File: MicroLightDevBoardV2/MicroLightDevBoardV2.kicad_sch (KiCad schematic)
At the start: 65 parts, among them J1 Conn_01x05_Socket, J10 Conn_01x01_Socket, J11 Conn_01x05_Socket, J12 Conn_01x02_Socket, J13 Conn_01x04_Socket, J14 Conn_01x04_Socket, J15 Conn_01x05_Socket, J16 Conn_01x01_Socket, J17 Conn_01x04_Socket, J18 Conn_01x04_Socket, J19 Conn_01x04_Socket, J2 Conn_01x05_Socket, J20 Conn_01x04_Socket, J21 Conn_01x04_Socket, J22 Conn_01x04_Socket, J23 Conn_01x03_Socket, J24 Conn_01x03_Socket, J25 Conn_01x04_Socket, J26 Conn_01x04_Socket, J27 Conn_01x02_Socket, J28 Conn_01x02_Socket, J29 Conn_01x02_Socket, J3 Conn_01x05_Socket, J30 Conn_01x02_Socket, J31 Conn_01x01_Socket, J32 Conn_01x06_Socket, J33 Conn_01x04_Socket, J4 Conn_01x05_Socket, J5 Conn_01x02_Socket, J6 Conn_01x02_Socket, J7 TYPE-C-31-M-12, J8 Conn_01x02_Socket, J9 Conn_01x02_Socket, U1 BQ25628RYKR, U2 ATtiny3226-M, U3 S-85S1AB33-I6T1U, U4 USBLC6-2P6, U5 MC3479

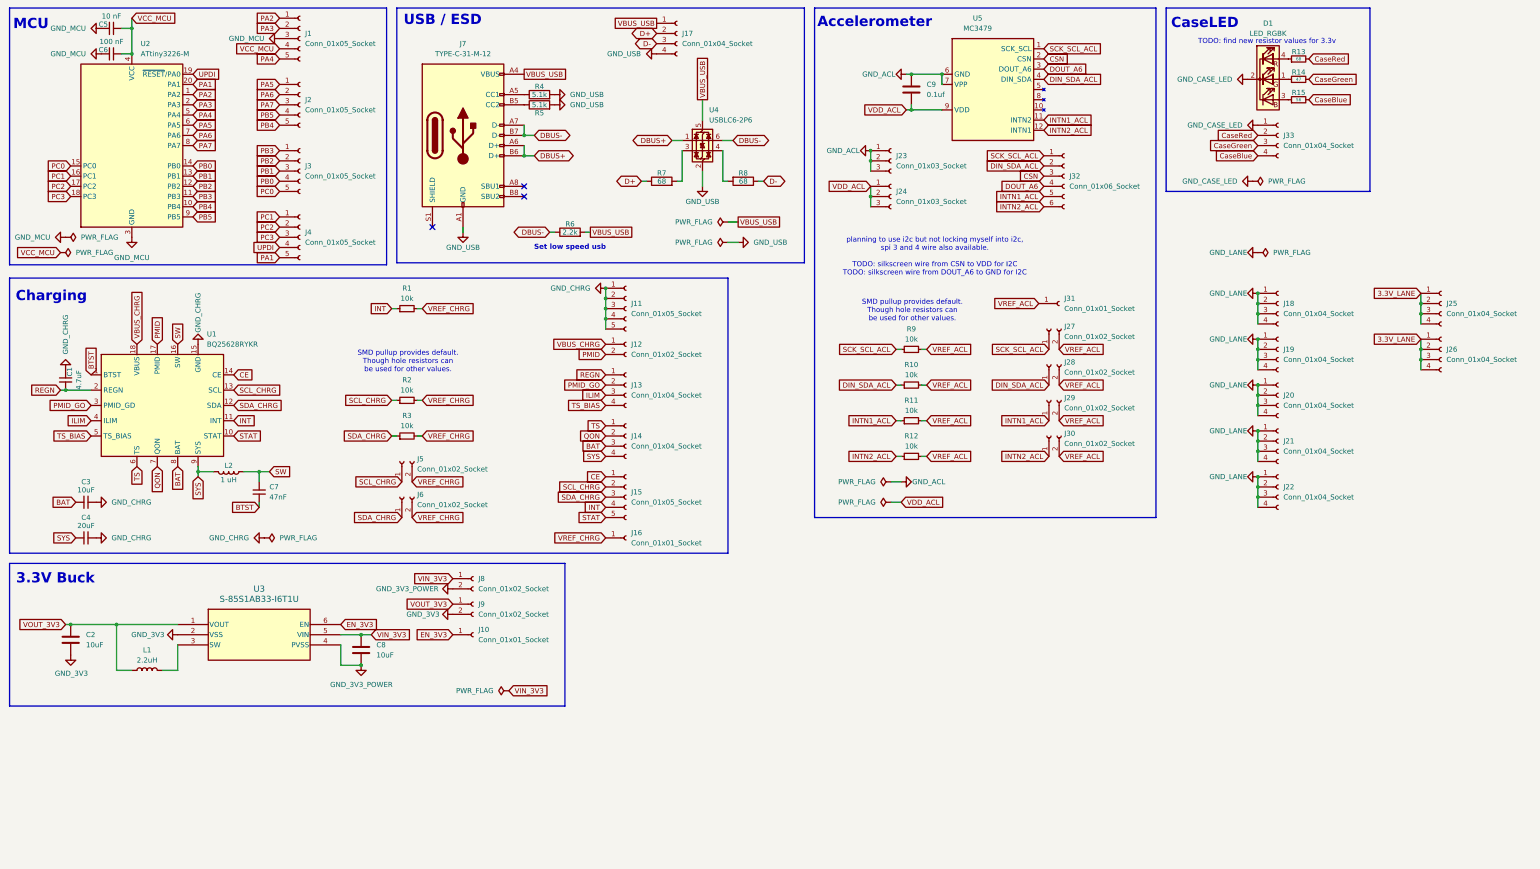
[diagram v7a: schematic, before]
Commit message: add buttons to pcb, add breadboard like expansion sockets
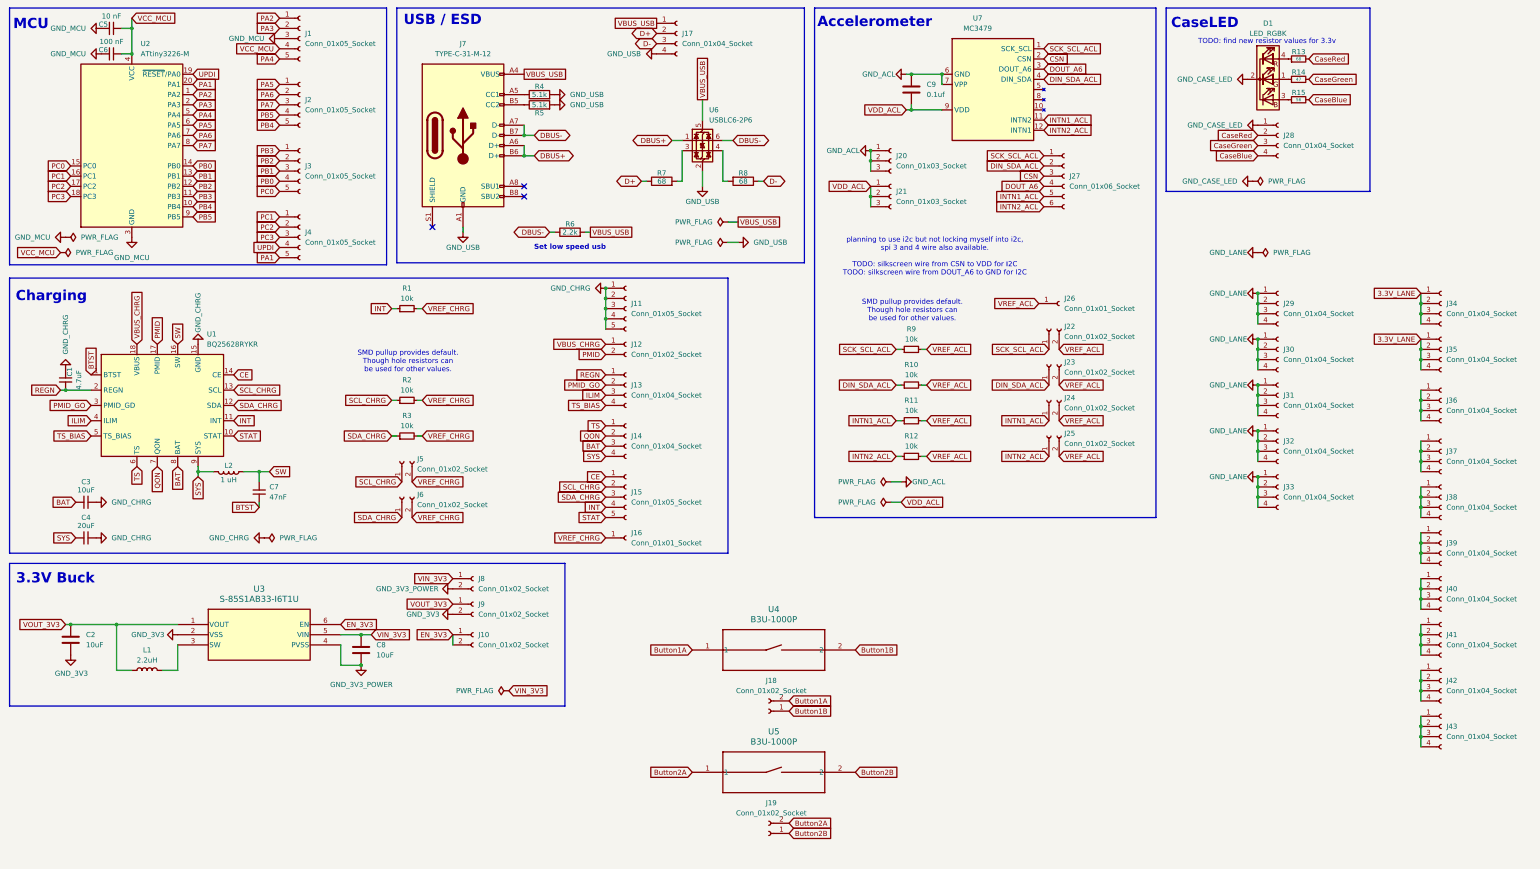
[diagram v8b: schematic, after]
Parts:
- removed J10: Conn_01x01_Socket, Connector_PinSocket_2.54mm:PinSocket_1x01_P2.54mm_Vertical, symbol Connector:Conn_01x01_Socket
- added J10, J18, J19: Conn_01x02_Socket, Connector_PinSocket_2.54mm:PinSocket_1x02_P2.54mm_Vertical, symbol Connector:Conn_01x02_Socket
- added J36, J37, J38, J39, J40, J41, J42, J43: Conn_01x04_Socket, Connector_PinSocket_2.54mm:PinSocket_1x04_P2.54mm_Vertical, symbol Connector:Conn_01x04_Socket
- added U4, U5: B3U-1000P, B3U-1000P, symbol MicroLightDevBoard:B3U-1000P
- renumbered J23 to J20, J24 to J21, J27 to J22, J28 to J23, J29 to J24, J30 to J25, J31 to J26, J32 to J27, J33 to J28, J18 to J29, J19 to J30, J20 to J31, J21 to J32, J22 to J33, J25 to J34, J26 to J35, U4 to U6, U5 to U7
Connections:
- net EN_3V3: now also J10.1 (Pin_1), J10.2 (Pin_2)
- new net: J41.1 (Pin_1), J41.2 (Pin_2), J41.3 (Pin_3), J41.4 (Pin_4)
- new net: J39.1 (Pin_1), J39.2 (Pin_2), J39.3 (Pin_3), J39.4 (Pin_4)
- new net: J38.1 (Pin_1), J38.2 (Pin_2), J38.3 (Pin_3), J38.4 (Pin_4)
- new net: J40.1 (Pin_1), J40.2 (Pin_2), J40.3 (Pin_3), J40.4 (Pin_4)
- new net: J36.1 (Pin_1), J36.2 (Pin_2), J36.3 (Pin_3), J36.4 (Pin_4)
- new net: J42.1 (Pin_1), J42.2 (Pin_2), J42.3 (Pin_3), J42.4 (Pin_4)
- new net: J37.1 (Pin_1), J37.2 (Pin_2), J37.3 (Pin_3), J37.4 (Pin_4)
- new net: J43.1 (Pin_1), J43.2 (Pin_2), J43.3 (Pin_3), J43.4 (Pin_4)
- new net Button1A: J18.2 (Pin_2), U4.1
- new net Button1B: J18.1 (Pin_1), U4.2
- new net Button2A: J19.2 (Pin_2), U5.1
- new net Button2B: J19.1 (Pin_1), U5.2
